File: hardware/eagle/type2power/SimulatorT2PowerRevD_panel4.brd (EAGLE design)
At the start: 99.1 x 99.1 mm, 37 parts

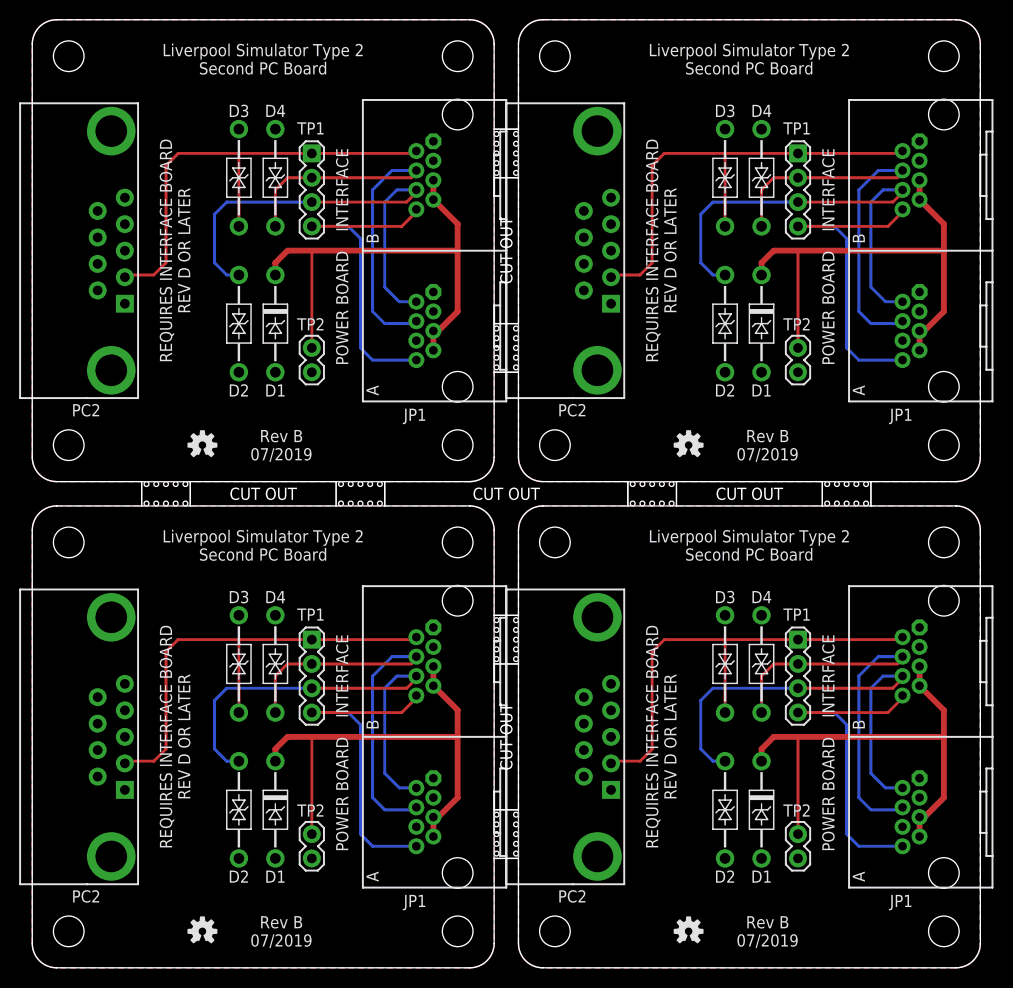
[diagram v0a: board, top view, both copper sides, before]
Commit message: Board Housekeeping
URL on silkscreens, caution messages, tidy up naming conventions.
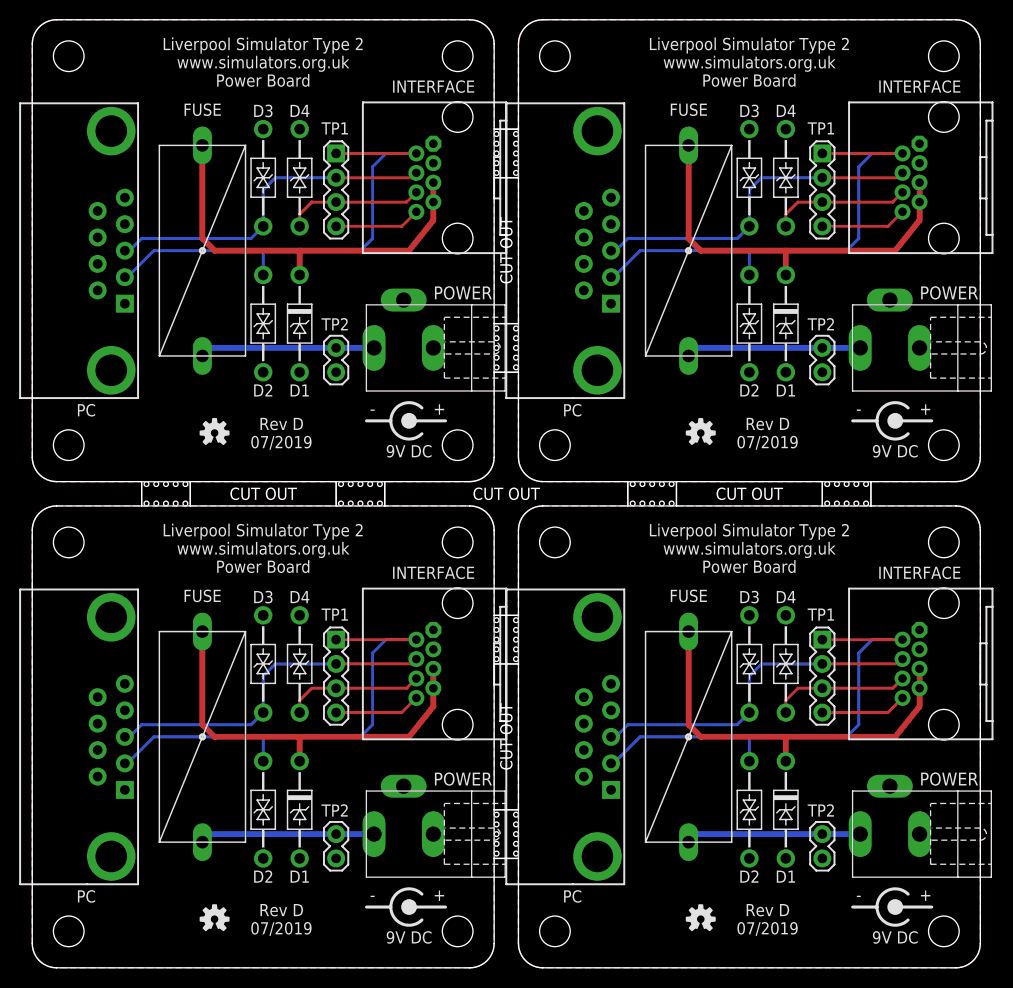
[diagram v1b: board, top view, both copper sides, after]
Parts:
- removed JP1, JP1_1, JP1_2, JP1_3: RJ45-RJHSE-5080-022HOLE, AIC_Custom:RJ45-RJHSE-5080-02
- added E$2: (no value), AIC_Custom:OUTLINE_PANEL_4_5MM
- added E$3, E$4, E$5: (no value), AIC_Custom:WARNING_TRIANGLE_TPLACE
- added FUSE, FUSE_1, FUSE_2, FUSE_3: 800mA, AIC_Custom:MCOMP-FUSE-HOLDER-PCB
- added INTERFACE, INTERFACE_1, INTERFACE_2, INTERFACE_3: RJ45-RJHSE-X08090DEG, AIC_Custom:RJ45-RJHSE-5080
- added POWER, POWER_1, POWER_2, POWER_3: 9V DC, AIC_Custom:CLIFF-FC681465P-DC-JACK
- added U$1, U$1_1, U$1_2, U$1_3: (no value), AIC_Custom:CENTRE-POS-SILK
- E$1: device AIC_Custom:OUTLINE_PANEL_4_5MM -> AIC_Custom:WARNING_TRIANGLE_TPLACE
- moved E$1 99.1 mm to (38.1, 91.4), flipped to the bottom
- moved D2_1 2.54 mm to (74.9, 16.5)
- moved D2_3 2.54 mm to (74.9, 67.3)
- moved D3_1 2.54 mm to (74.9, 31.8)
- moved D3_3 2.54 mm to (74.9, 82.5)
- moved D1 2.54 mm to (27.9, 16.5)
- moved D1_2 2.54 mm to (27.9, 67.3)
- moved D4 2.54 mm to (27.9, 31.8)
- moved D4_2 2.54 mm to (27.9, 82.5)
- moved D2 2.54 mm to (24.1, 16.5)
- moved D2_2 2.54 mm to (24.1, 67.3)
- moved D3 2.54 mm to (24.1, 31.8)
- moved D3_2 2.54 mm to (24.1, 82.5)
- moved TP1 2.54 mm to (31.8, 34.3)
- moved TP1_2 2.54 mm to (31.8, 85.1)
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- renumbered PC2 to PC, PC2_1 to PC_1, PC2_2 to PC_2, PC2_3 to PC_3
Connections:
- new net VIN: FUSE.2, POWER.1, TP2.1
- new net VIN1: FUSE_1.2, POWER_1.1, TP2_1.1
- new net VIN3: FUSE_2.2, POWER_2.1, TP2_2.1
- new net VIN4: FUSE_3.2, POWER_3.1, TP2_3.1
- net GND: now also INTERFACE.1, INTERFACE.3, POWER.3; no longer JP1.A1, JP1.A3, JP1.B1, JP1.B3
- net GND1: now also INTERFACE_1.1, INTERFACE_1.3, POWER_1.3; no longer JP1_1.A1, JP1_1.A3, JP1_1.B1, JP1_1.B3
- net GND2: now also INTERFACE_2.1, INTERFACE_2.3, POWER_2.3; no longer JP1_2.A1, JP1_2.A3, JP1_2.B1, JP1_2.B3
- net GND3: now also INTERFACE_3.1, INTERFACE_3.3, POWER_3.3; no longer JP1_3.A1, JP1_3.A3, JP1_3.B1, JP1_3.B3
- net P8: now also INTERFACE.8; no longer JP1.A8, JP1.B8
- net P81: now also INTERFACE_1.8; no longer JP1_1.A8, JP1_1.B8
- net P82: now also INTERFACE_2.8; no longer JP1_2.A8, JP1_2.B8
- net P83: now also INTERFACE_3.8; no longer JP1_3.A8, JP1_3.B8
- net RXD: now also D3.C, INTERFACE.4, PC.3; no longer D4.C, JP1.A4, JP1.B4
- net RXD1: now also D3_1.C, INTERFACE_1.4, PC_1.3; no longer D4_1.C, JP1_1.A4, JP1_1.B4
- net RXD2: now also D3_2.C, INTERFACE_2.4, PC_2.3; no longer D4_2.C, JP1_2.A4, JP1_2.B4
- net RXD3: now also D3_3.C, INTERFACE_3.4, PC_3.3; no longer D4_3.C, JP1_3.A4, JP1_3.B4
- net TX2: now also D4.C, INTERFACE.6; no longer D2.C, JP1.A2, JP1.B6
- net TX21: now also D4_1.C, INTERFACE_1.6; no longer D2_1.C, JP1_1.A2, JP1_1.B6
- net TX22: now also D4_2.C, INTERFACE_2.6; no longer D2_2.C, JP1_2.A2, JP1_2.B6
- net TX23: now also D4_3.C, INTERFACE_3.6; no longer D2_3.C, JP1_3.A2, JP1_3.B6
- net TXD: now also D2.C, INTERFACE.2; no longer D3.C, JP1.B2
- net TXD1: now also D2_1.C, INTERFACE_1.2; no longer D3_1.C, JP1_1.B2
- net TXD2: now also D2_2.C, INTERFACE_2.2; no longer D3_2.C, JP1_2.B2
- net TXD3: now also D2_3.C, INTERFACE_3.2; no longer D3_3.C, JP1_3.B2
- net VIN2: now also FUSE.1, INTERFACE.5, INTERFACE.7; no longer JP1.A5, JP1.A7, JP1.B5, JP1.B7, TP2.1
- net VIN21: now also FUSE_1.1, INTERFACE_1.5, INTERFACE_1.7; no longer JP1_1.A5, JP1_1.A7, JP1_1.B5, JP1_1.B7, TP2_1.1
- net VIN22: now also FUSE_2.1, INTERFACE_2.5, INTERFACE_2.7; no longer JP1_2.A5, JP1_2.A7, JP1_2.B5, JP1_2.B7, TP2_2.1
- net VIN23: now also FUSE_3.1, INTERFACE_3.5, INTERFACE_3.7; no longer JP1_3.A5, JP1_3.A7, JP1_3.B5, JP1_3.B7, TP2_3.1
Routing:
- net TX21: track 47.1 -> 14.4 mm
- net TX23: track 47.1 -> 14.4 mm
- net TX2: track 47.1 -> 14.4 mm
- net TX22: track 47.1 -> 14.4 mm
- net P82: track 35.2 -> 9.01 mm
- net P83: track 35.2 -> 9.01 mm
- net P8: track 35.2 -> 9.01 mm
- net P81: track 35.2 -> 9.01 mm
- net VIN1: track 0.00 -> 18.3 mm
- net VIN4: track 0.00 -> 18.3 mm
- net VIN: track 0.00 -> 18.3 mm
- net VIN3: track 0.00 -> 18.3 mm
- net VIN22: track 51.2 -> 42.4 mm
- net VIN23: track 51.2 -> 42.4 mm
- net VIN2: track 51.2 -> 42.4 mm
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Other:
- board text added: "Connect this board to Liverpool Simulator Type 2 or compatible equipment ONLY. Refer to documentation for details."
- board text added: "FUSE"
- board text added: "INTERFACE"
- board text added: "Liverpool Simulator Type 2 www.simulators.org.uk Power Board"
- board text added: "PC"
- board text added: "POWER"
- board text added: "Rev D 07/2019"
- board text removed: "JP1"
- board text removed: "Liverpool Simulator Type 2 Second PC Board"
- board text removed: "PC2"
- board text removed: "POWER BOARD INTERFACE"
- board text removed: "REQUIRES INTERFACE BOARD REV D OR LATER"
- board text removed: "Rev B 07/2019"
